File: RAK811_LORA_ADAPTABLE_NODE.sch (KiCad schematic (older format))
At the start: 41 parts, among them J1 Screw_Terminal_01x02, J10 Conn_01x01_Male, J11 Conn_01x01_Male, J12 Conn_01x01_Male, J13 Conn_01x01_Male, J14 Conn_01x01_Male, J15 Conn_01x01_Male, J16 Conn_01x01_Male, J17 Conn_01x01_Male, J18 Conn_01x01_Male, J19 Conn_01x01_Male, J2 Screw_Terminal_01x03, J20 Conn_01x01_Male, J21 Conn_01x01_Male, J22 Conn_01x01_Male, J23 Conn_01x01_Male, J24 Conn_01x01_Male, J25 Conn_01x01_Male, J26 Conn_01x01_Male, J27 Conn_01x01_Male, J28 Conn_01x01_Male, J29 Conn_01x01_Male, J3 Conn_01x01_Male, J30 Conn_01x01_Male, J31 Conn_01x01_Male, J32 Conn_01x01_Male, J4 Conn_01x01_Male, J5 Conn_01x01_Male, J6 Conn_01x01_Male, J7 Conn_Coaxial, J8 Conn_01x01_Male, J9 Conn_01x01_Male, U1 RAK811-HF

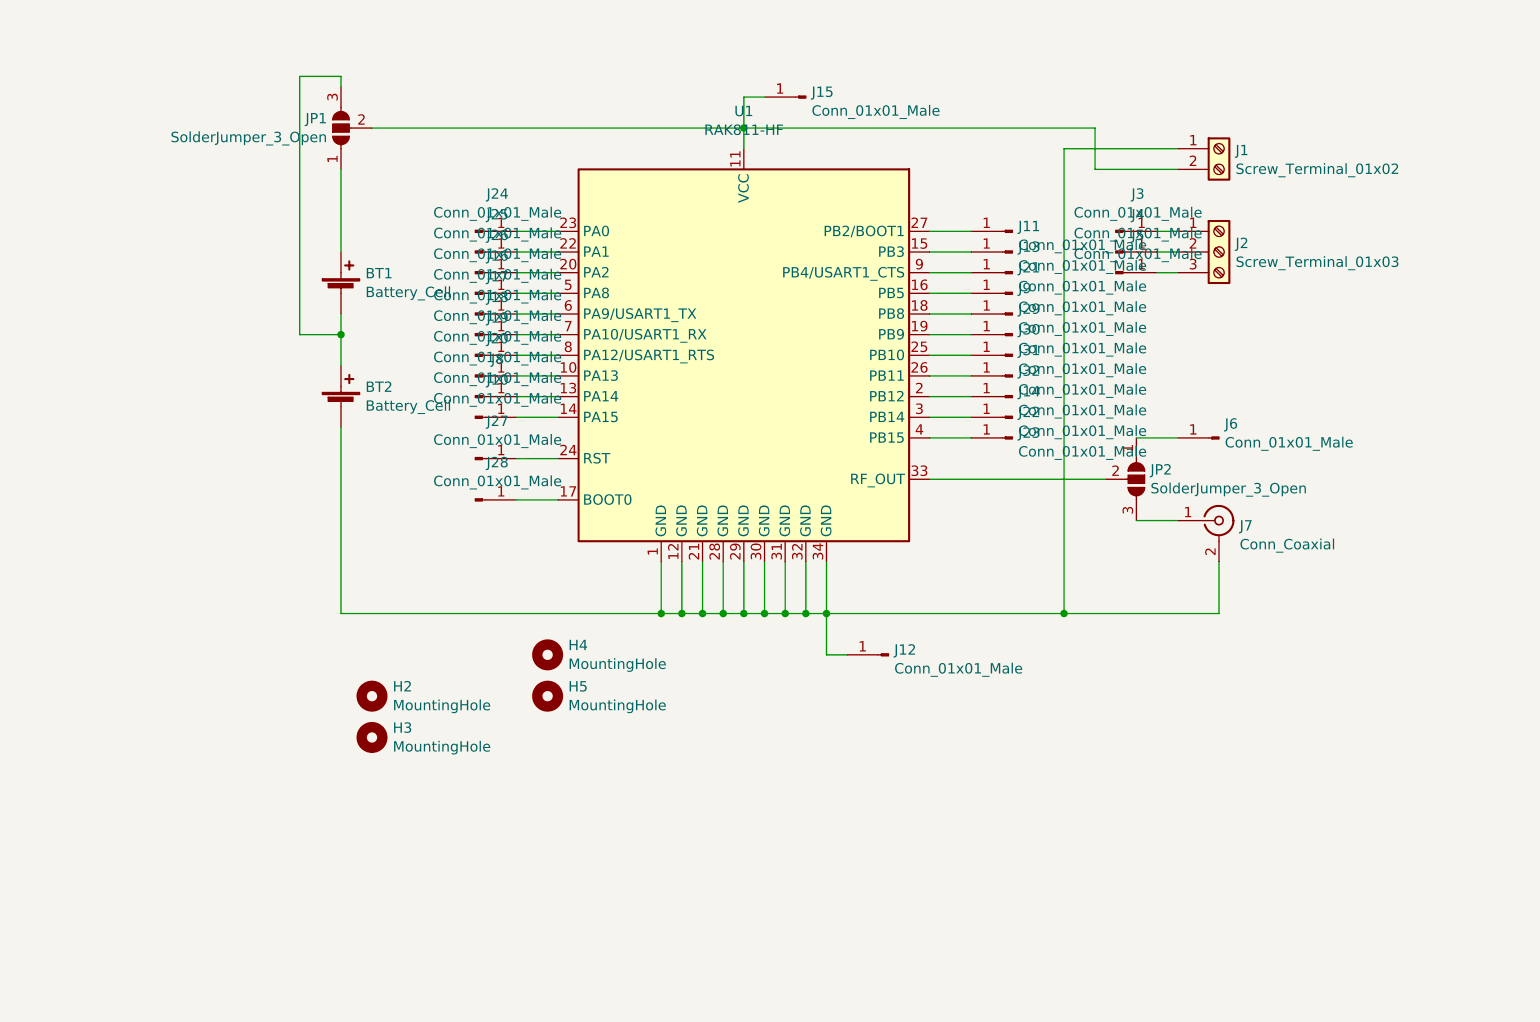
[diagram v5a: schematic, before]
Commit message: 3 of 4 i/o connectors changed from individual to row
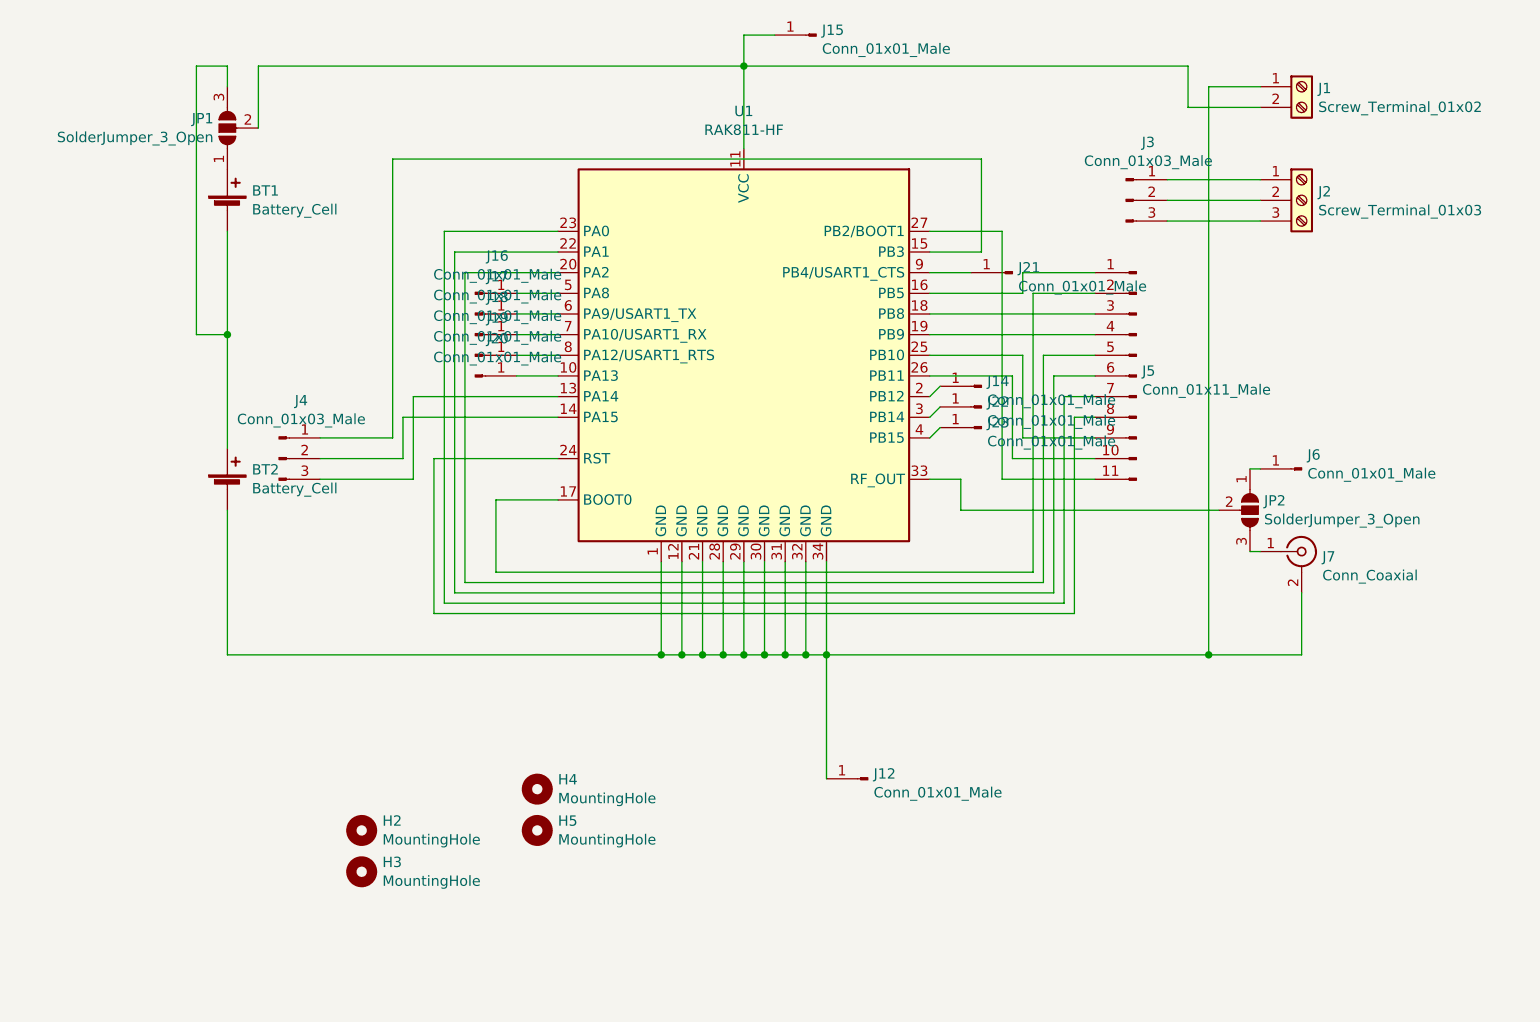
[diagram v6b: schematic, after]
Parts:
- removed J10, J11, J13, J24, J25, J26, J27, J28, J29, J3, J30, J31, J32, J4, J5, J8, J9: Conn_01x01_Male, Connector_Wire:SolderWirePad_1x01_Drill0.8mm, symbol Connector:Conn_01x01_Male
- added J3, J4: Conn_01x03_Male, Connector_PinHeader_2.54mm:PinHeader_1x03_P2.54mm_Vertical, symbol Connector:Conn_01x03_Male
- added J5: Conn_01x11_Male, Connector_PinHeader_2.54mm:PinHeader_1x11_P2.54mm_Vertical, symbol Connector:Conn_01x11_Male
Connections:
- net at U1.13 (PA14): now also J4.3 (Pin_3)
- net at U1.14 (PA15): now also J4.2 (Pin_2)
- net at U1.15 (PB3): now also J4.1 (Pin_1)
- net at U1.16 (PB5): now also J5.1 (Pin_1)
- net at U1.17 (BOOT0): now also J5.2 (Pin_2)
- net at U1.18 (PB8): now also J5.3 (Pin_3)
- net at U1.19 (PB9): now also J5.4 (Pin_4)
- net at U1.20 (PA2): now also J5.5 (Pin_5)
- net at U1.22 (PA1): now also J5.6 (Pin_6)
- net at U1.23 (PA0): now also J5.7 (Pin_7)
- net at U1.24 (RST): now also J5.8 (Pin_8)
- net at U1.25 (PB10): now also J5.9 (Pin_9)
- net at U1.26 (PB11): now also J5.10 (Pin_10)
- net at U1.27 (PB2/BOOT1): now also J5.11 (Pin_11)
- net at J2.1 (Pin_1): now also J3.1 (Pin_1)
- net at J2.2 (Pin_2): now also J3.2 (Pin_2)
- net at J2.3 (Pin_3): now also J3.3 (Pin_3)
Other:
- moved on the sheet: BT1, BT2, H2, H3, H4, H5, J1, J12, J14, J15, J2, J22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

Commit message: all i/o routed, some battery fine tuning traces todo
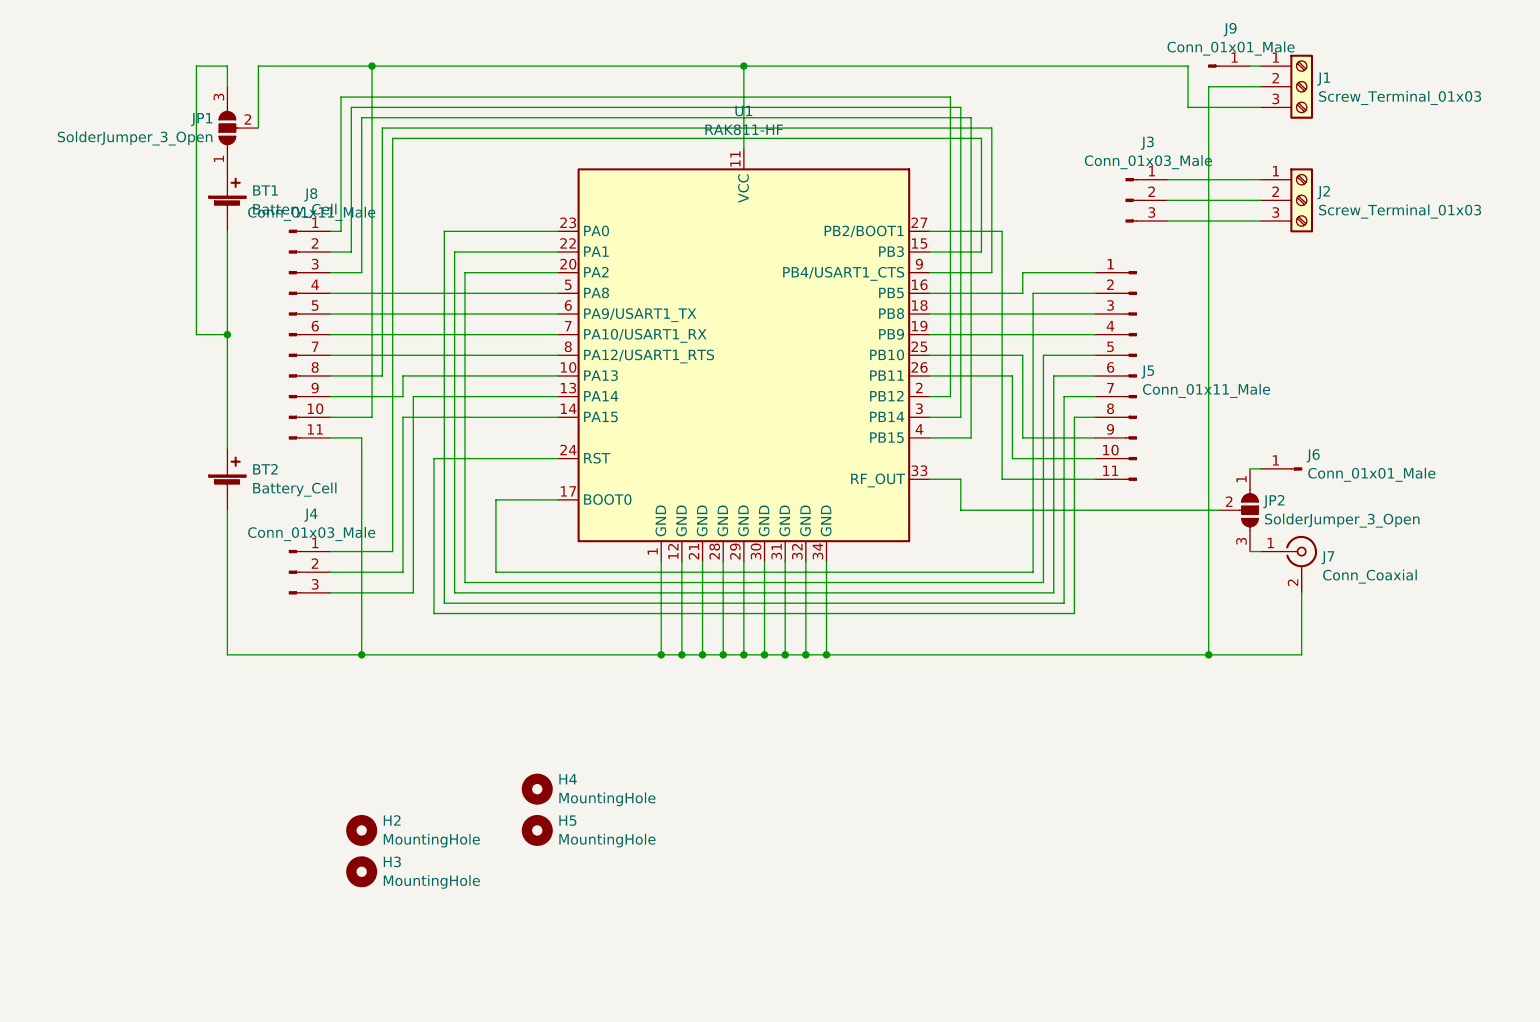
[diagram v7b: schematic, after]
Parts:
- removed J1: Screw_Terminal_01x02, TerminalBlock_4Ucon:TerminalBlock_4Ucon_1x02_P3.50mm_Horizontal, symbol Connector:Screw_Terminal_01x02
- removed J12, J14, J15, J16, J17, J18, J19, J20, J21, J22, J23: Conn_01x01_Male, Connector_Wire:SolderWirePad_1x01_Drill0.8mm, symbol Connector:Conn_01x01_Male
- added J1: Screw_Terminal_01x03, TerminalBlock_4Ucon:TerminalBlock_4Ucon_1x03_P3.50mm_Horizontal, symbol Connector:Screw_Terminal_01x03
- added J8: Conn_01x11_Male, Connector_PinHeader_2.54mm:PinHeader_1x11_P2.54mm_Vertical, symbol Connector:Conn_01x11_Male
- added J9: Conn_01x01_Male, Connector_PinHeader_2.54mm:PinHeader_1x01_P2.54mm_Vertical, symbol Connector:Conn_01x01_Male
- J6: footprint Connector_Wire:SolderWirePad_1x01_Drill0.8mm -> Connector_PinHeader_2.54mm:PinHeader_1x01_P2.54mm_Vertical
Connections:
- net at BT2.2 (-), J7.2 (Ext), U1.1 (GND)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: now also J1.2 (Pin_2), J8.11 (Pin_11)
- net at U1.10 (PA13): now also J8.9 (Pin_9)
- net at JP1.2 (C), U1.11 (VCC): now also J1.3 (Pin_3), J8.10 (Pin_10)
- net at U1.2 (PB12): now also J8.1 (Pin_1)
- net at U1.3 (PB14): now also J8.2 (Pin_2)
- net at U1.4 (PB15): now also J8.3 (Pin_3)
- net at U1.5 (PA8): now also J8.4 (Pin_4)
- net at U1.6 (PA9/USART1_TX): now also J8.5 (Pin_5)
- net at U1.7 (PA10/USART1_RX): now also J8.6 (Pin_6)
- net at U1.8 (PA12/USART1_RTS): now also J8.7 (Pin_7)
- net at U1.9 (PB4/USART1_CTS): now also J8.8 (Pin_8)
- new net: J1.1 (Pin_1), J9.1 (Pin_1)
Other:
- moved on the sheet: J4

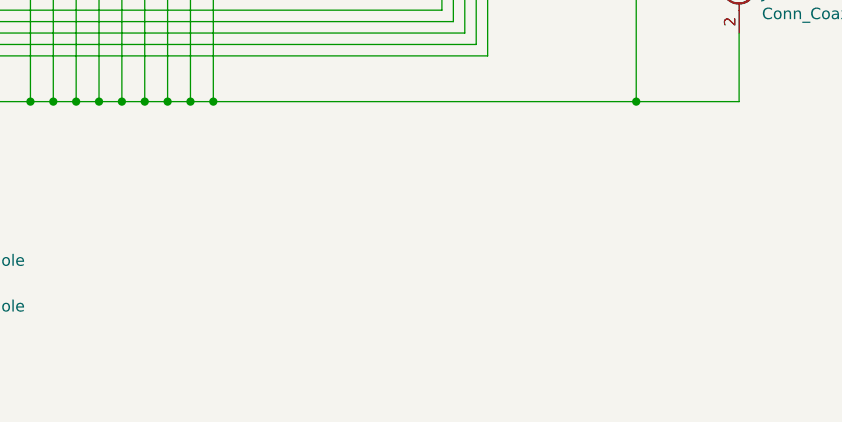
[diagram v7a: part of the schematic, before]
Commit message: all traces routed
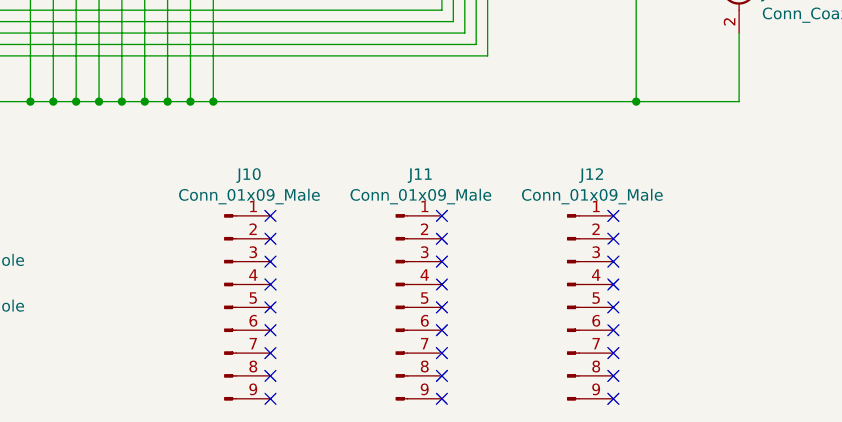
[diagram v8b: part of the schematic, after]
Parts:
- added J10, J11, J12: Conn_01x09_Male, Connector_PinHeader_2.54mm:PinHeader_1x09_P2.54mm_Vertical, symbol Connector:Conn_01x09_Male
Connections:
- no-connect marks 0 -> 27
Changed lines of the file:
@@
 Wire Wire Line
 	7900 1550 7950 1550
+$Comp
+L Connector:Conn_01x09_Male J11
+U 1 1 5EFBD325
+P 6650 5300
+F 0 "J11" H 6758 5881 50  0000 C CNN
+F 1 "Conn_01x09_Male" H 6758 5790 50  0000 C CNN
+F 2 "Connector_PinHeader_2.54mm:PinHeader_1x09_P2.54mm_Vertical" H 6650 5300 50  0001 C CNN
+F 3 "~" H 6650 5300 50  0001 C CNN
+	1    6650 5300
+	1    0    0    -1
+$EndComp
+$Comp
+L Connector:Conn_01x09_Male J10
+U 1 1 5EFBF61F
+P 5900 5300
+F 0 "J10" H 6008 5881 50  0000 C CNN
+F 1 "Conn_01x09_Male" H 6008 5790 50  0000 C CNN
+F 2 "Connector_PinHeader_2.54mm:PinHeader_1x09_P2.54mm_Vertical" H 5900 5300 50  0001 C CNN
+F 3 "~" H 5900 5300 50  0001 C CNN
+	1    5900 5300
+	1    0    0    -1
+$EndComp
+$Comp
+L Connector:Conn_01x09_Male J12
+U 1 1 5EFC1064
+P 7400 5300
+F 0 "J12" H 7508 5881 50  0000 C CNN
+F 1 "Conn_01x09_Male" H 7508 5790 50  0000 C CNN
+F 2 "Connector_PinHeader_2.54mm:PinHeader_1x09_P2.54mm_Vertical" H 7400 5300 50  0001 C CNN
+F 3 "~" H 7400 5300 50  0001 C CNN
+	1    7400 5300
+	1    0    0    -1
+$EndComp
+NoConn ~ 7600 4900
+NoConn ~ 7600 5000
+NoConn ~ 7600 5100
+NoConn ~ 7600 5200
+NoConn ~ 7600 5300
+NoConn ~ 7600 5400
+NoConn ~ 7600 5500
+NoConn ~ 7600 5600
+NoConn ~ 7600 5700
+NoConn ~ 6850 5700
+NoConn ~ 6850 5600
+NoConn ~ 6850 5500
+NoConn ~ 6850 5400
+NoConn ~ 6850 5300
+NoConn ~ 6850 5200
+NoConn ~ 6850 5100
+NoConn ~ 6850 5000
+NoConn ~ 6850 4900
+NoConn ~ 6100 4900
+NoConn ~ 6100 5000
+NoConn ~ 6100 5100
+NoConn ~ 6100 5200
+NoConn ~ 6100 5300
+NoConn ~ 6100 5400
+NoConn ~ 6100 5500
+NoConn ~ 6100 5600
+NoConn ~ 6100 5700
 $EndSCHEMATC
